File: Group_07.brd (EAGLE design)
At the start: 62.2 x 74.9 mm, 29 parts, among them J1 POWER_JACKPTH_LOCK, U1 +12v, U3 TCA9546ASO16, U4 TMUX1208

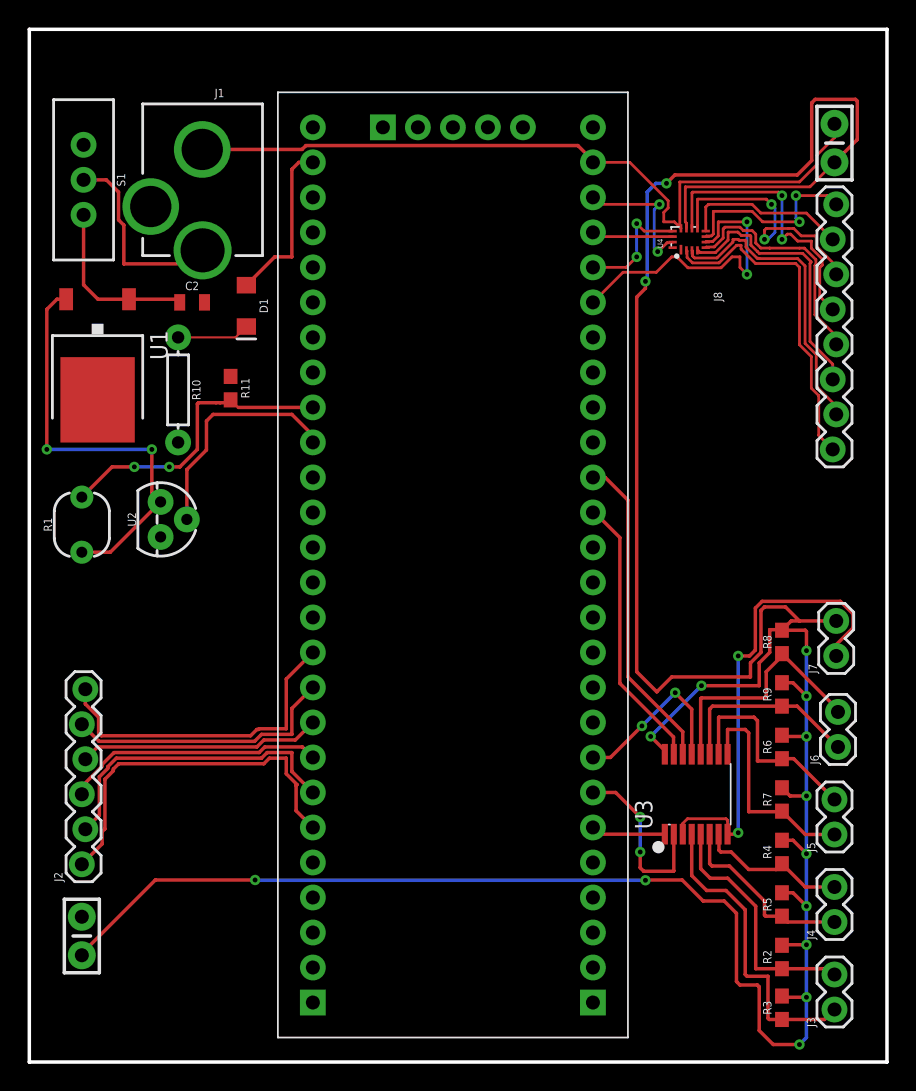
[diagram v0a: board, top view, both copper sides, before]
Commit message: aggiunta primi nomi componenti, holes e modifica descrizione DRC
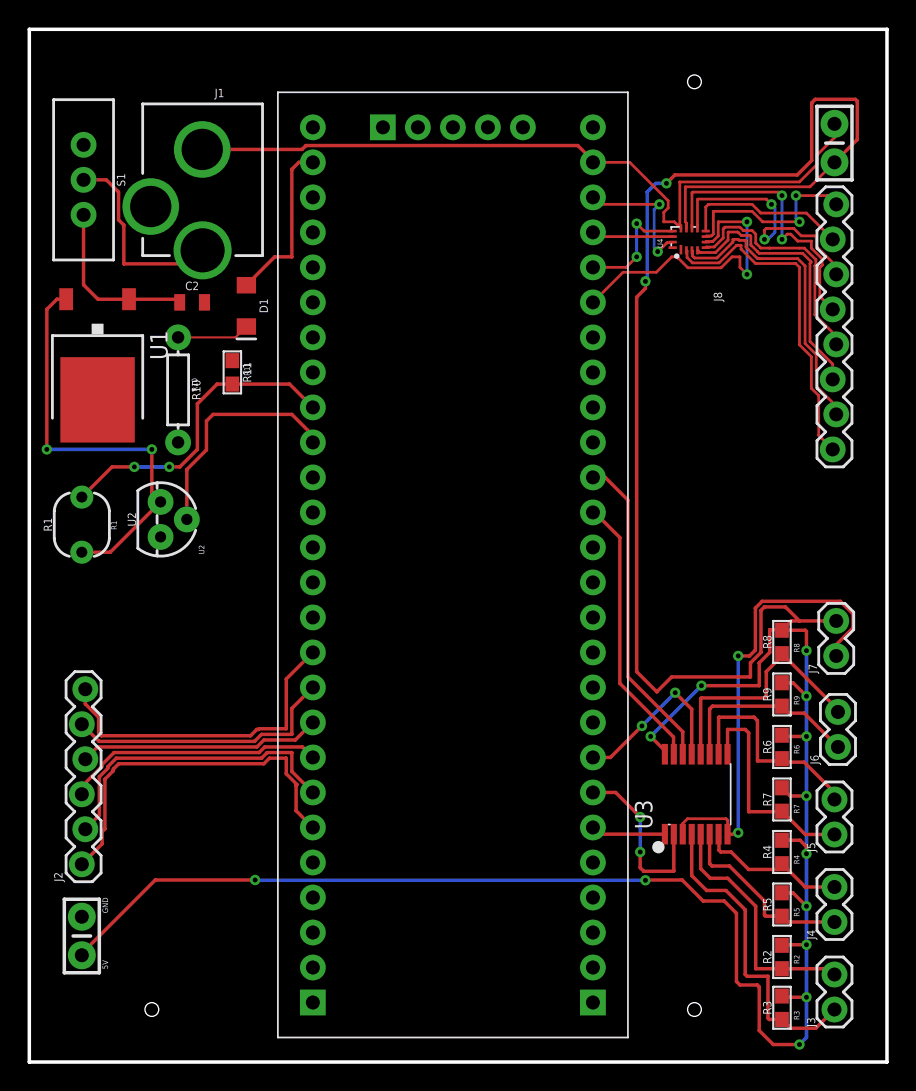
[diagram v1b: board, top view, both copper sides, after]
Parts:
- moved R11 1.15 mm to (14.7, 50.0)
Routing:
- net PHOTO_OUT: track 22.0 -> 22.8 mm
- net I2C_SDA_0: track 22.5 -> 23.0 mm
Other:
- board text added: "5V"
- board text added: "GND"
- board text added: "R1"
- board text added: "R10"
- board text added: "R11"
- board text added: "R2"
- board text added: "R3"
- board text added: "R4"
- board text added: "R5"
- board text added: "R6"
- board text added: "R7"
- board text added: "R8"
- board text added: "R9"
- board text added: "U2"

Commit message: Silkscreen
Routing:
- net GND: track 90.7 -> 179.0 mm, vias 2 -> 8
- net 5V: track 255.6 -> 303.0 mm, vias 17 -> 19
- net I2C_SCL_3: track 18.3 -> 19.7 mm
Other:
- board text added: "0.1uF"
- board text added: "0.33µF"
- board text added: "10k"
- board text added: "330"
- board text added: "4.7K"
- board text added: "BLUE LED"
- board text added: "C1"
- board text added: "C3"
- board text added: "OFF"
- board text added: "ON"
- board text added: "PHOTOCELLPTH"
- board text added: "POWER"
- board text added: "TEMPERATURE SENSOR"
- board text removed: "R1"
- board text removed: "R10"
- board text removed: "R11"
- board text removed: "R2"
- board text removed: "R3"
- board text removed: "R4"
- board text removed: "R5"
- board text removed: "R6"
- board text removed: "R7"
- board text removed: "R8"
- board text removed: "R9"
- board text removed: "U2"

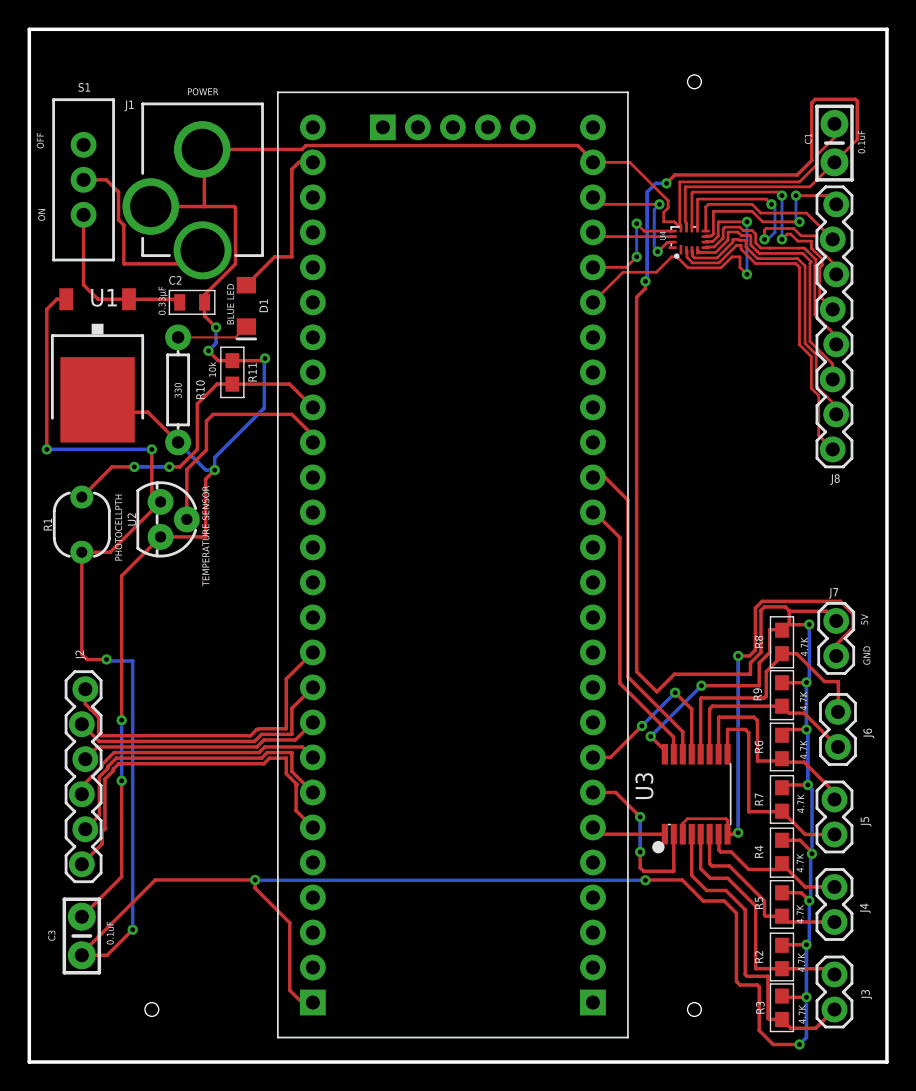
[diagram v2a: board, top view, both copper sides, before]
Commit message: riduzione dimensioni board e riposizionamento componenti con verifica dru
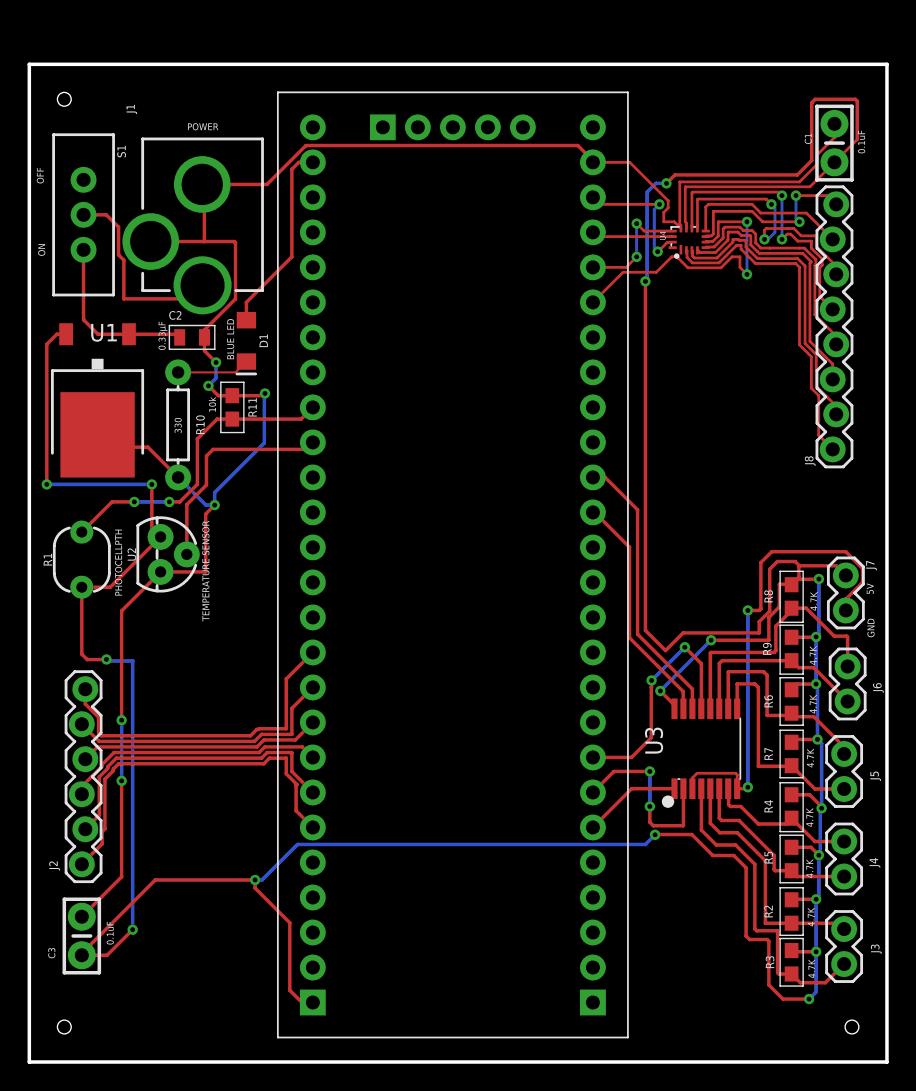
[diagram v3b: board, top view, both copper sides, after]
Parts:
- moved J7 3.37 mm to (59.2, 32.8)
- moved J6 3.37 mm to (59.4, 26.2)
- moved R5 3.37 mm to (55.3, 14.7)
- moved R6 3.37 mm to (55.3, 26.2)
- moved R7 3.37 mm to (55.3, 22.4)
- moved R8 3.37 mm to (55.3, 33.8)
- moved U3 3.37 mm to (49.1, 22.7)
- moved R3 3.37 mm to (55.3, 7.24)
- moved R2 3.37 mm to (55.3, 10.9)
- moved R4 3.37 mm to (55.3, 18.5)
- moved J4 3.37 mm to (59.1, 13.5)
- moved J3 3.37 mm to (59.1, 7.11)
- moved R9 3.37 mm to (55.3, 30.0)
- moved J5 3.37 mm to (59.1, 19.8)
- moved J1 2.54 mm to (12.6, 70.2)
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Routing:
- net I2C_A2: track 12.9 -> 17.4 mm
- net 5V: track 303.0 -> 299.5 mm
- net I2C_SCL: track 23.3 -> 20.3 mm
- net I2C_SDA: track 20.1 -> 17.0 mm
- net N$9: track 12.2 -> 14.0 mm
- net I2C_A0: track 5.42 -> 7.08 mm
- net GND: track 179.0 -> 178.0 mm
- net TEMP_OUT: track 16.8 -> 15.9 mm
- net I2C_A1: track 13.1 -> 13.7 mm
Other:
- board size 62.2 x 74.9 mm -> 62.2 x 72.4 mm

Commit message: Modifica silkscreen, mask and DRC check
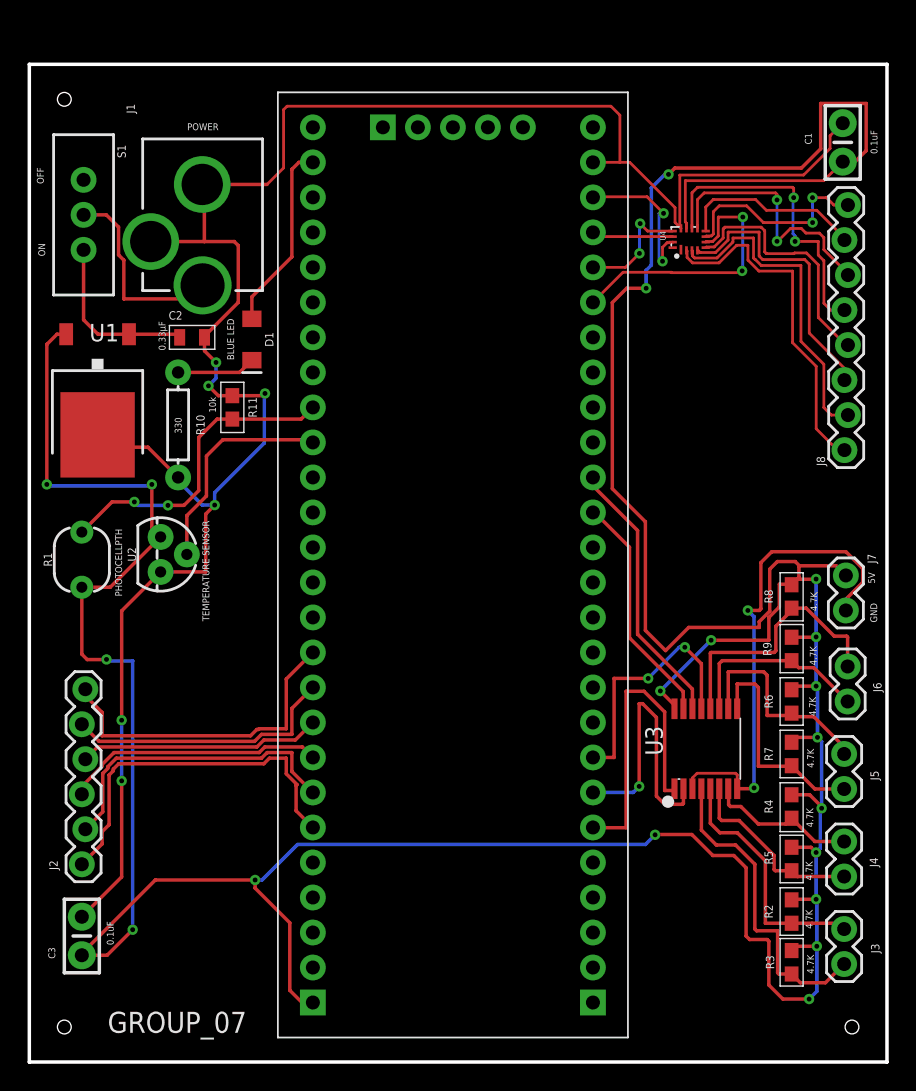
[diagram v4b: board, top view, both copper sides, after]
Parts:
- moved J8 0.85 mm to (59.3, 62.2)
- moved C1 0.60 mm to (59.0, 66.7)
- moved D1 0.41 mm to (16.1, 52.4)
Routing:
- net I2C_A0: track 7.08 -> 22.2 mm
- net GND: track 178.0 -> 187.4 mm
- net I2C_A1: track 13.7 -> 20.2 mm, vias 2 -> 1
- net 5V: track 299.5 -> 302.8 mm
- net MUX_OUT/1.4C: track 22.2 -> 20.0 mm
- net N$11: track 22.1 -> 23.8 mm
- net MUX_A0/1.3C: track 10.1 -> 11.6 mm
- net N$14: track 20.7 -> 22.1 mm
- net N$16: track 12.1 -> 13.3 mm
- net I2C_A2: track 17.4 -> 18.3 mm
- net N$13: track 17.2 -> 18.0 mm
- net N$12: track 19.8 -> 20.6 mm
- net N$2: track 24.4 -> 25.1 mm
- net N$17: track 14.0 -> 14.7 mm
- net PHOTO_OUT: track 22.4 -> 23.0 mm
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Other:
- board text added: "GROUP_07"

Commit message: Holes e controllo traces
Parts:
- moved J1 3.71 mm to (12.5, 73.9)
- moved J8 2.54 mm to (59.3, 59.6)
- moved U4 2.54 mm to (47.9, 57.1)
- moved C1 2.54 mm to (59.0, 64.2)
- moved C2 2.47 mm to (11.2, 55.0)
- moved R10 2.27 mm to (10.2, 48.4)
- moved R11 0.26 mm to (14.5, 47.6)
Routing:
- net GND: track 187.4 -> 193.2 mm
- net N$1: track 14.4 -> 10.9 mm
- net 5V: track 302.8 -> 300.8 mm, vias 19 -> 17
- net MUX_A1/1.4C: track 5.91 -> 6.96 mm
- net MUX_A0/1.3C: track 11.6 -> 12.6 mm
- net MUX_OUT/1.4C: track 20.0 -> 19.3 mm
- net N$10: track 5.72 -> 6.45 mm
